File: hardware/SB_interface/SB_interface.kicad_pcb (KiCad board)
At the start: 2 copper layers, 235 parts, among them J1 8P8C_TelPairs, J2 8P8C_TelPairs, J3 8P8C_TelPairs, J4 Conn_01x10_Pin, J5 Screw_Terminal_01x02, J6 Screw_Terminal_01x02, J7 Jack-DC, K1 J104D2C12VDC.36S, K10 J104D2C12VDC.36S, K11 J104D2C12VDC.36S, K12 J104D2C12VDC.36S, K13 J104D2C12VDC.36S, K2 J104D2C12VDC.36S, K3 J104D2C12VDC.36S, K4 J104D2C12VDC.36S, K5 J104D2C12VDC.36S, K6 J104D2C12VDC.36S, K7 J104D2C12VDC.36S, K8 J104D2C12VDC.36S, K9 J104D2C12VDC.36S, Q1 2N7002, Q10 2N7002, Q11 2N7002, Q12 2N7002, Q13 2N7002, Q14 MMBTA42, Q15 MMBTA42, Q16 MMBTA42, Q17 MMBTA42, Q18 MMBTA42, Q19 MMBTA42, Q2 2N7002, Q20 MMBTA42, Q21 MMBTA42, Q22 MMBTA42, Q23 MMBTA42, Q24 MMBTA42, Q25 MMBTA42, Q26 MMBTA42, Q27 MMBTA42, Q28 MMBTA42, Q29 MMBTA42, Q3 2N7002, Q30 MMBTA42, Q31 MMBTA42, Q32 MMBTA42, Q33 MMBTA42, Q34 MMBTA42, Q35 MMBTA42, Q36 MMBTA42, Q37 MMBTA42, Q4 2N7002, Q5 2N7002, Q6 2N7002, Q7 2N7002, Q8 2N7002, Q9 2N7002, U1 MCP23017_SP, U2 MCP23017_SP

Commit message: replicated layout + added JLCPCB Design rules file
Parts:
- removed D50, D55, D60: 1N4148WS, Diode_SMD:D_SOD-323
- removed D51, D56, D61: Yellow, PCM_JLCPCB:D_0805
- removed D54, D59: 1SMA4729A, PCM_JLCPCB:D_SMA
- removed JP16, JP18: SolderJumper_2_Bridged, Jumper:SolderJumper-2_P1.3mm_Bridged_Pad1.0x1.5mm
- removed JP17, JP19, JP20: SolderJumper_2_Open, Jumper:SolderJumper-2_P1.3mm_Open_Pad1.0x1.5mm
- removed R77, R78, R79, R80, R81, R82, R83, R84, R85, R86, R87, R88: 2.2kΩ, PCM_JLCPCB:R_0805
- added C13: C, Capacitor_SMD:C_0805_2012Metric_Pad1.18x1.45mm_HandSolder, F.Cu at (185.8, 127.2)
- added C14: C, Capacitor_SMD:C_0805_2012Metric_Pad1.18x1.45mm_HandSolder, F.Cu at (165.7, 57.4)
- added D32: 1N4148WS, Diode_SMD:D_SOD-323, F.Cu at (133.4, 196.2)
- added D33: Yellow, PCM_JLCPCB:D_0805, F.Cu at (130.5, 194.1)
- added D37: Yellow, PCM_JLCPCB:D_0805, F.Cu at (15.5, 133.6)
- added D38: 1SMA4729A, PCM_JLCPCB:D_SMA, F.Cu at (87.2, 151.0)
- added D42: 1SMA4729A, PCM_JLCPCB:D_SMA, F.Cu at (155.0, 125.8)
- added D43: 1SMA4729A, PCM_JLCPCB:D_SMA, F.Cu at (155.0, 132.4)
- added D47: 1SMA4729A, PCM_JLCPCB:D_SMA, F.Cu at (135.0, 62.6)
- added D48: 1N4148WS, Diode_SMD:D_SOD-323, F.Cu at (128.9, 59.1)
- added JP10: Jumper_2_Small_Open, Connector_PinHeader_2.54mm:PinHeader_1x02_P2.54mm_Vertical, F.Cu at (9.97, -88.8)
- added JP11: Jumper_2_Small_Open, Connector_PinHeader_2.54mm:PinHeader_1x02_P2.54mm_Vertical, F.Cu at (14.6, -88.8)
- added JP12: Jumper_2_Small_Open, Connector_PinHeader_2.54mm:PinHeader_1x02_P2.54mm_Vertical, F.Cu at (0.67, -81.6)
- added JP13: Jumper_2_Small_Open, Connector_PinHeader_2.54mm:PinHeader_1x02_P2.54mm_Vertical, F.Cu at (5.32, -81.6)
- added JP14: Jumper_2_Small_Open, Connector_PinHeader_2.54mm:PinHeader_1x02_P2.54mm_Vertical, F.Cu at (9.97, -81.6)
- added R42: 180Ω, PCM_JLCPCB:R_2010, F.Cu at (119.6, 252.2)
- added R43: 180Ω, PCM_JLCPCB:R_2010, F.Cu at (113.1, 252.2)
- added R46: 2.2kΩ, PCM_JLCPCB:R_0805, F.Cu at (87.3, 261.4)
- added R47: 470kΩ, PCM_JLCPCB:R_0805, F.Cu at (158.0, 197.9)
- added R48: 180Ω, PCM_JLCPCB:R_2010, F.Cu at (162.8, 190.2)
- added R51: 4.7kΩ, PCM_JLCPCB:R_0805, F.Cu at (122.1, 196.2)
- added R52: 2.2kΩ, PCM_JLCPCB:R_0805, F.Cu at (130.5, 199.4)
- added R53: 470kΩ, PCM_JLCPCB:R_0805, F.Cu at (43.0, 137.4)
- added R56: R, Resistor_SMD:R_0805_2012Metric_Pad1.20x1.40mm_HandSolder, F.Cu at (52.3, 134.1)
- added R57: 4.7kΩ, PCM_JLCPCB:R_0805, F.Cu at (7.11, 135.7)
- added R58: 2.2kΩ, PCM_JLCPCB:R_0805, F.Cu at (15.5, 138.9)
- added R64: 2.2kΩ, PCM_JLCPCB:R_0805, F.Cu at (78.2, 157.2)
- C1, C2: value C -> 100nF; footprint Capacitor_SMD:C_0805_2012Metric_Pad1.18x1.45mm_HandSolder -> PCM_JLCPCB:C_0805
- D10, D15, D30, D35: value 1N4148WS -> 1SMA4729A; footprint Diode_SMD:D_SOD-323 -> PCM_JLCPCB:D_SMA
- D11, D26, D31, D46: value Yellow -> 1SMA4729A; footprint PCM_JLCPCB:D_0805 -> PCM_JLCPCB:D_SMA
- D12, D24, D28, D4, D44: value 1SMA4729A -> 1N4148WS; footprint PCM_JLCPCB:D_SMA -> Diode_SMD:D_SOD-323
- D13, D17, D29, D49, D5: value 1SMA4729A -> Yellow; footprint PCM_JLCPCB:D_SMA -> PCM_JLCPCB:D_0805
- D16, D36: value Yellow -> 1N4148WS; footprint PCM_JLCPCB:D_0805 -> Diode_SMD:D_SOD-323
- D25, D45: value 1N4148WS -> Yellow; footprint Diode_SMD:D_SOD-323 -> PCM_JLCPCB:D_0805
- J4: value Conn_01x10_Pin -> Screw_Terminal_01x02; footprint Connector_PinHeader_2.54mm:PinHeader_1x10_P2.54mm_Vertical -> TerminalBlock_Phoenix:TerminalBlock_Phoenix_PT-1,5-2-3.5-H_1x02_P3.50mm_Horizontal
- J6: value Screw_Terminal_01x02 -> Conn_01x10_Pin; footprint TerminalBlock_Phoenix:TerminalBlock_Phoenix_PT-1,5-2-3.5-H_1x02_P3.50mm_Horizontal -> Connector_PinHeader_2.54mm:PinHeader_1x10_P2.54mm_Vertical
- JP1: value SolderJumper_2_Bridged -> SolderJumper_2_Open; footprint Jumper:SolderJumper-2_P1.3mm_Bridged_Pad1.0x1.5mm -> Jumper:SolderJumper-2_P1.3mm_Open_Pad1.0x1.5mm
- JP15, JP5, JP8: value SolderJumper_2_Bridged -> Jumper_2_Small_Open; footprint Jumper:SolderJumper-2_P1.3mm_Bridged_Pad1.0x1.5mm -> Connector_PinHeader_2.54mm:PinHeader_1x02_P2.54mm_Vertical
- JP4, JP6, JP7, JP9: value SolderJumper_2_Open -> Jumper_2_Small_Open; footprint Jumper:SolderJumper-2_P1.3mm_Open_Pad1.0x1.5mm -> Connector_PinHeader_2.54mm:PinHeader_1x02_P2.54mm_Vertical
- K10, K11, K12, K13, K2, K4, K5, K6, K7, K8, K9: moved to B.Cu
- Q11, Q12, Q2, Q3, Q5, Q6, Q8, Q9: value 2N7002 -> MMBTA42
- Q16, Q19, Q22, Q25, Q28, Q31, Q34, Q37: value MMBTA42 -> 2N7002
- R10, R40: value 4.7kΩ -> 2.2kΩ
- R11, R17, R23, R41, R5: value 180Ω -> 470kΩ; footprint PCM_JLCPCB:R_2010 -> PCM_JLCPCB:R_0805
- R16, R22, R28: value 180Ω -> 2.2kΩ; footprint PCM_JLCPCB:R_2010 -> PCM_JLCPCB:R_0805
- R19, R24, R49, R54, R7: value R -> 180Ω; footprint Resistor_SMD:R_0805_2012Metric_Pad1.20x1.40mm_HandSolder -> PCM_JLCPCB:R_2010
- R2, R3: value 180Ω -> 1kΩ; footprint PCM_JLCPCB:R_2010 -> PCM_JLCPCB:R_0805
- R20, R50, R8: value 4.7kΩ -> R; footprint PCM_JLCPCB:R_0805 -> Resistor_SMD:R_0805_2012Metric_Pad1.20x1.40mm_HandSolder
- R21, R27, R33, R9: value 180Ω -> 4.7kΩ; footprint PCM_JLCPCB:R_2010 -> PCM_JLCPCB:R_0805
- R25, R30, R55: value 4.7kΩ -> 180Ω; footprint PCM_JLCPCB:R_0805 -> PCM_JLCPCB:R_2010
- R26, R32, R38: value 180Ω -> R; footprint PCM_JLCPCB:R_2010 -> Resistor_SMD:R_0805_2012Metric_Pad1.20x1.40mm_HandSolder
- R29, R59: value R -> 470kΩ; footprint Resistor_SMD:R_0805_2012Metric_Pad1.20x1.40mm_HandSolder -> PCM_JLCPCB:R_0805
- R34: value R -> 2.2kΩ; footprint Resistor_SMD:R_0805_2012Metric_Pad1.20x1.40mm_HandSolder -> PCM_JLCPCB:R_0805
- R35: value 4.7kΩ -> 470kΩ
- R39: value R -> 4.7kΩ; footprint Resistor_SMD:R_0805_2012Metric_Pad1.20x1.40mm_HandSolder -> PCM_JLCPCB:R_0805
- R4: value R -> 1kΩ; footprint Resistor_SMD:R_0805_2012Metric_Pad1.20x1.40mm_HandSolder -> PCM_JLCPCB:R_0805
- R60, R61: value 1kΩ -> 180Ω; footprint PCM_JLCPCB:R_0805 -> PCM_JLCPCB:R_2010
- R62: value 1kΩ -> R; footprint PCM_JLCPCB:R_0805 -> Resistor_SMD:R_0805_2012Metric_Pad1.20x1.40mm_HandSolder
- R66, R67, R72, R73: value 470kΩ -> 180Ω; footprint PCM_JLCPCB:R_0805 -> PCM_JLCPCB:R_2010
- R68, R74: value 470kΩ -> R; footprint PCM_JLCPCB:R_0805 -> Resistor_SMD:R_0805_2012Metric_Pad1.20x1.40mm_HandSolder
- R69, R75: value 470kΩ -> 4.7kΩ
- R70, R76: value 470kΩ -> 2.2kΩ
- moved C3 341.4 mm to (261.4, 26.1), turned to 90 degrees
- moved R5 334.8 mm to (249.2, 29.3)
- moved Q5 332.3 mm to (273.0, 142.9), turned to -90 degrees
- moved R14 321.9 mm to (282.2, 142.8), turned to -90 degrees
- moved C4 321.4 mm to (285.1, 142.8), turned to 90 degrees
- moved K7 317.5 mm to (-46.4, 259.2), turned to 180 degrees
- moved Q4 317.2 mm to (217.4, 27.7)
- moved Q19 316.6 mm to (-51.0, 255.1)
- moved D13 315.0 mm to (-45.1, 165.0), turned to -90 degrees
- moved D23 310.7 mm to (-37.8, 258.7)
- moved D4 309.5 mm to (224.5, 27.7), turned to 90 degrees
- moved R6 303.9 mm to (254.0, 21.7), turned to 180 degrees
- moved C6 302.0 mm to (-13.8, 86.9), turned to 90 degrees
- moved DB6 301.5 mm to (-27.7, 255.4), turned to 90 degrees
- moved D6 297.8 mm to (254.3, 141.4)
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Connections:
- C1 pad 1: /RING_1 -> +3.3V
- C10 pad 1: /RING_9 -> /RING_7
- C11 pad 1: /RING_10 -> /RING_8
- C12 pad 1: /RING_11 -> /RING_9
- C2 pad 1: /RING_0 -> +3.3V
- C3 pad 1: /RING_2 -> /RING_1
- C4 pad 1: /RING_3 -> /RING_0
- C5 pad 1: /RING_4 -> /RING_2
- C6 pad 1: /RING_5 -> /RING_3
- C7 pad 1: /RING_6 -> /RING_4
- C8 pad 1: /RING_7 -> /RING_5
- C9 pad 1: /RING_8 -> /RING_6
- D10 pad 1: +12V -> /RelayAndRingDetect2/Tel_B
- D10 pad 2: Net-(D10-A) -> Net-(D10-Pad2)
- D11 pad 1: Net-(D10-A) -> /RelayAndRingDetect2/Tel_A
- D12 pad 1: /RelayAndRingDetect4/Tel_B -> +12V
- D12 pad 2: Net-(D12-Pad2) -> Net-(D12-A)
- D13 pad 1: /RelayAndRingDetect5/Tel_B -> Net-(D12-A)
- D14 pad 1: /RelayAndRingDetect2/Tel_A -> /RelayAndRingDetect3/Tel_B
- D15 pad 1: +12V -> /RelayAndRingDetect3/Tel_A
- D15 pad 2: Net-(D15-A) -> Net-(D15-Pad2)
- D16 pad 1: Net-(D15-A) -> +12V
- D16 pad 2: Net-(D16-Pad2) -> Net-(D16-A)
- D17 pad 1: /RelayAndRingDetect6/Tel_B -> Net-(D16-A)
- D18 pad 1: /RelayAndRingDetect7/Tel_B -> /RelayAndRingDetect4/Tel_B
- D19 pad 1: /RelayAndRingDetect3/Tel_A -> /RelayAndRingDetect4/Tel_A
- D22 pad 1: /RelayAndRingDetect8/Tel_B -> /RelayAndRingDetect5/Tel_B
- D23 pad 1: /RelayAndRingDetect9/Tel_B -> /RelayAndRingDetect5/Tel_A
- D24 pad 1: /RelayAndRingDetect4/Tel_A -> +12V
- D24 pad 2: Net-(D24-Pad2) -> Net-(D24-A)
- D25 pad 1: +12V -> Net-(D24-A)
- D25 pad 2: Net-(D25-A) -> Net-(D25-Pad2)
- D26 pad 1: Net-(D25-A) -> /RelayAndRingDetect6/Tel_B
- D27 pad 1: /RelayAndRingDetect10/Tel_B -> /RelayAndRingDetect6/Tel_A
- D28 pad 1: /RelayAndRingDetect11/Tel_B -> +12V
- D28 pad 2: Net-(D28-Pad2) -> Net-(D28-A)
- D29 pad 1: /RelayAndRingDetect5/Tel_A -> Net-(D28-A)
- D3 pad 1: /RelayAndRingDetect0/Tel_B -> /RelayAndRingDetect1/Tel_A
- D30 pad 1: +12V -> /RelayAndRingDetect7/Tel_B
- D30 pad 2: Net-(D30-A) -> Net-(D30-Pad2)
- D31 pad 1: Net-(D30-A) -> /RelayAndRingDetect7/Tel_A
- D34 pad 1: /RelayAndRingDetect6/Tel_A -> /RelayAndRingDetect8/Tel_B
- D35 pad 1: +12V -> /RelayAndRingDetect8/Tel_A
- D35 pad 2: Net-(D35-A) -> Net-(D35-Pad2)
- D36 pad 1: Net-(D35-A) -> +12V
- D36 pad 2: Net-(D36-Pad2) -> Net-(D36-A)
- D39 pad 1: /RelayAndRingDetect7/Tel_A -> /RelayAndRingDetect9/Tel_A
- D4 pad 1: /RelayAndRingDetect2/Tel_B -> +12V
- D4 pad 2: Net-(D4-Pad2) -> Net-(D4-A)
- D44 pad 1: /RelayAndRingDetect8/Tel_A -> +12V
- D44 pad 2: Net-(D44-Pad2) -> Net-(D44-A)
- D45 pad 1: +12V -> Net-(D44-A)
- D45 pad 2: Net-(D45-A) -> Net-(D45-Pad2)
- D46 pad 1: Net-(D45-A) -> /RelayAndRingDetect11/Tel_B
- D49 pad 1: /RelayAndRingDetect9/Tel_A -> Net-(D48-A)
- D5 pad 1: /RelayAndRingDetect1/Tel_A -> Net-(D4-A)
- D6 pad 1: /RelayAndRingDetect3/Tel_B -> /RelayAndRingDetect0/Tel_B
- DB1 pad 4: Net-(D5-Pad2) -> Net-(D3-Pad2)
- DB10 pad 3: Net-(D23-Pad2) -> Net-(D38-Pad2)
- DB10 pad 4: Net-(D49-Pad2) -> Net-(D39-Pad2)
- DB11 pad 3: Net-(D27-Pad2) -> Net-(D42-Pad2)
- DB12 pad 3: Net-(D28-Pad2) -> Net-(D46-Pad2)
- DB2 pad 3: Net-(D3-Pad2) -> Net-(D6-Pad2)
- DB3 pad 3: Net-(D4-Pad2) -> Net-(D10-Pad2)
- DB3 pad 4: Net-(D14-Pad2) -> Net-(D11-Pad2)
- DB4 pad 3: Net-(D6-Pad2) -> Net-(D14-Pad2)
- DB4 pad 4: Net-(D19-Pad2) -> Net-(D15-Pad2)
- DB5 pad 3: Net-(D12-Pad2) -> Net-(D18-Pad2)
- DB5 pad 4: Net-(D24-Pad2) -> Net-(D19-Pad2)
- DB6 pad 3: Net-(D13-Pad2) -> Net-(D22-Pad2)
- DB6 pad 4: Net-(D29-Pad2) -> Net-(D23-Pad2)
- DB7 pad 3: Net-(D17-Pad2) -> Net-(D26-Pad2)
- DB7 pad 4: Net-(D34-Pad2) -> Net-(D27-Pad2)
- DB8 pad 3: Net-(D18-Pad2) -> Net-(D30-Pad2)
- DB8 pad 4: Net-(D39-Pad2) -> Net-(D31-Pad2)
- DB9 pad 3: Net-(D22-Pad2) -> Net-(D34-Pad2)
- DB9 pad 4: Net-(D44-Pad2) -> Net-(D35-Pad2)
- J4 pad 1: /SDA -> /AUX_A
- J4 pad 2: /SCL -> /AUX_B
- J6 pad 1: /AUX_A -> /SDA
- J6 pad 2: /AUX_B -> /SCL
- JP1 pad 1: +3.3V -> /INTB_1
- JP1 pad 2: Net-(JP1-B) -> /INTA_1
- JP15 pad 1: Net-(JP15-A) -> GND
- JP15 pad 2: GND -> Net-(JP14-A)
- JP2 pad 1: /INTB_1 -> /INTA_2
- JP2 pad 2: /INTA_1 -> /INTB_1
- JP3 pad 1: GND -> /INTB_2
- JP3 pad 2: Net-(JP1-B) -> /INTA_2
- JP4 pad 1: /INTA_2 -> Net-(JP4-A)
- JP4 pad 2: /INTB_1 -> +3.3V
- JP5 pad 1: +3.3V -> GND
- JP5 pad 2: Net-(JP5-B) -> Net-(JP4-A)
- JP6 pad 1: /INTB_2 -> Net-(JP6-A)
- JP6 pad 2: /INTA_2 -> +3.3V
- JP7 pad 2: Net-(JP5-B) -> Net-(JP6-A)
- JP8 pad 1: +3.3V -> Net-(JP8-A)
- JP8 pad 2: Net-(JP8-B) -> +3.3V
- JP9 pad 2: Net-(JP8-B) -> Net-(JP8-A)
- K10 pad A2: Net-(D45-A) -> Net-(D36-A)
- K11 pad A2: Net-(D50-A) -> Net-(D40-A)
- K12 pad A2: Net-(D55-A) -> Net-(D44-A)
- K13 pad A2: Net-(D60-A) -> Net-(D48-A)
- K2 pad A2: Net-(D10-A) -> Net-(D4-A)
- K4 pad A2: Net-(D15-A) -> Net-(D12-A)
- K5 pad A2: Net-(D20-A) -> Net-(D16-A)
- K6 pad A2: Net-(D25-A) -> Net-(D20-A)
- K7 pad A2: Net-(D30-A) -> Net-(D24-A)
- K8 pad A2: Net-(D35-A) -> Net-(D28-A)
- K9 pad A2: Net-(D40-A) -> Net-(D32-A)
- Q10 pad 1: /SEL_PORT_8 -> /SEL_PORT_2
- Q10 pad 3: Net-(D45-A) -> Net-(D12-A)
- Q11 pad 1: /SEL_PORT_9 -> Net-(Q11-B)
- Q11 pad 2: GND -> Net-(DB4--)
- Q11 pad 3: Net-(D50-A) -> Net-(Q11-C)
- Q12 pad 1: /SEL_PORT_10 -> Net-(Q11-C)
- Q12 pad 2: GND -> Net-(Q11-B)
- Q12 pad 3: Net-(D55-A) -> Net-(OP4-CAT)
- Q13 pad 1: /SEL_PORT_11 -> /SEL_PORT_3
- Q13 pad 3: Net-(D60-A) -> Net-(D16-A)
- Q14 pad 2: Net-(Q14-E) -> Net-(DB5--)
- Q14 pad 3: Net-(OP1-CAT) -> Net-(Q14-C)
- Q15 pad 1: Net-(Q15-B) -> Net-(Q14-C)
- Q15 pad 2: Net-(Q15-E) -> Net-(Q14-B)
- Q15 pad 3: Net-(OP2-CAT) -> Net-(OP5-CAT)
- Q16 pad 1: Net-(Q16-B) -> /SEL_PORT_4
- Q16 pad 2: Net-(Q16-E) -> GND
- Q16 pad 3: Net-(OP3-CAT) -> Net-(D20-A)
- Q17 pad 2: Net-(Q17-E) -> Net-(DB6--)
- Q17 pad 3: Net-(OP4-CAT) -> Net-(Q17-C)
- Q18 pad 1: Net-(Q18-B) -> Net-(Q17-C)
- Q18 pad 2: Net-(Q18-E) -> Net-(Q17-B)
- Q18 pad 3: Net-(OP5-CAT) -> Net-(OP6-CAT)
- Q19 pad 1: Net-(Q19-B) -> /SEL_PORT_5
- Q19 pad 2: Net-(Q19-E) -> GND
- Q19 pad 3: Net-(OP6-CAT) -> Net-(D24-A)
- Q2 pad 1: /SEL_PORT_1 -> Net-(Q2-B)
- Q2 pad 2: GND -> Net-(DB1--)
- Q2 pad 3: Net-(D10-A) -> Net-(Q2-C)
- Q20 pad 2: Net-(Q20-E) -> Net-(DB7--)
- Q20 pad 3: Net-(OP7-CAT) -> Net-(Q20-C)
- Q21 pad 1: Net-(Q21-B) -> Net-(Q20-C)
- Q21 pad 2: Net-(Q21-E) -> Net-(Q20-B)
- Q21 pad 3: Net-(OP8-CAT) -> Net-(OP7-CAT)
- Q22 pad 1: Net-(Q22-B) -> /SEL_PORT_6
- Q22 pad 2: Net-(Q22-E) -> GND
- Q22 pad 3: Net-(OP9-CAT) -> Net-(D28-A)
- Q23 pad 2: Net-(Q23-E) -> Net-(DB8--)
- Q23 pad 3: Net-(OP10-CAT) -> Net-(Q23-C)
- Q24 pad 1: Net-(Q24-B) -> Net-(Q23-C)
- Q24 pad 2: Net-(Q24-E) -> Net-(Q23-B)
- Q24 pad 3: Net-(OP11-CAT) -> Net-(OP8-CAT)
- Q25 pad 1: Net-(Q25-B) -> /SEL_PORT_7
- Q25 pad 2: Net-(Q25-E) -> GND
- Q25 pad 3: Net-(OP12-CAT) -> Net-(D32-A)
- Q26 pad 1: Net-(Q14-E) -> Net-(Q26-B)
- Q26 pad 2: Net-(DB1--) -> Net-(DB9--)
- Q26 pad 3: Net-(Q14-B) -> Net-(Q26-C)
- Q27 pad 1: Net-(Q15-E) -> Net-(Q26-C)
- Q27 pad 2: Net-(DB2--) -> Net-(Q26-B)
- Q27 pad 3: Net-(Q15-B) -> Net-(OP9-CAT)
- Q28 pad 1: Net-(Q16-E) -> /SEL_PORT_8
- Q28 pad 2: Net-(DB3--) -> GND
- Q28 pad 3: Net-(Q16-B) -> Net-(D36-A)
- Q29 pad 1: Net-(Q17-E) -> Net-(Q29-B)
- Q29 pad 2: Net-(DB4--) -> Net-(DB10--)
- Q29 pad 3: Net-(Q17-B) -> Net-(Q29-C)
- Q3 pad 1: /SEL_PORT_0 -> Net-(Q2-C)
- Q3 pad 2: GND -> Net-(Q2-B)
- Q3 pad 3: Net-(D8-A) -> Net-(OP1-CAT)
- Q30 pad 1: Net-(Q18-E) -> Net-(Q29-C)
- Q30 pad 2: Net-(DB5--) -> Net-(Q29-B)
- Q30 pad 3: Net-(Q18-B) -> Net-(OP10-CAT)
- Q31 pad 1: Net-(Q19-E) -> /SEL_PORT_9
- Q31 pad 2: Net-(DB6--) -> GND
- Q31 pad 3: Net-(Q19-B) -> Net-(D40-A)
- Q32 pad 1: Net-(Q20-E) -> Net-(Q32-B)
- Q32 pad 2: Net-(DB7--) -> Net-(DB11--)
- Q32 pad 3: Net-(Q20-B) -> Net-(Q32-C)
- Q33 pad 1: Net-(Q21-E) -> Net-(Q32-C)
- Q33 pad 2: Net-(DB8--) -> Net-(Q32-B)
- Q33 pad 3: Net-(Q21-B) -> Net-(OP11-CAT)
- Q34 pad 1: Net-(Q22-E) -> /SEL_PORT_10
- Q34 pad 2: Net-(DB9--) -> GND
- Q34 pad 3: Net-(Q22-B) -> Net-(D44-A)
- Q35 pad 1: Net-(Q23-E) -> Net-(Q35-B)
- Q35 pad 2: Net-(DB10--) -> Net-(DB12--)
- Q35 pad 3: Net-(Q23-B) -> Net-(Q35-C)
- Q36 pad 1: Net-(Q24-E) -> Net-(Q35-C)
- Q36 pad 2: Net-(DB11--) -> Net-(Q35-B)
- Q36 pad 3: Net-(Q24-B) -> Net-(OP12-CAT)
- Q37 pad 1: Net-(Q25-E) -> /SEL_PORT_11
- Q37 pad 2: Net-(DB12--) -> GND
- Q37 pad 3: Net-(Q25-B) -> Net-(D48-A)
- Q4 pad 1: /SEL_PORT_2 -> /SEL_PORT_1
- Q4 pad 3: Net-(D15-A) -> Net-(D4-A)
- Q5 pad 1: /SEL_PORT_3 -> Net-(Q5-B)
- Q5 pad 2: GND -> Net-(DB2--)
- Q5 pad 3: Net-(D20-A) -> Net-(Q5-C)
- Q6 pad 1: /SEL_PORT_4 -> Net-(Q5-C)
- Q6 pad 2: GND -> Net-(Q5-B)
- Q6 pad 3: Net-(D25-A) -> Net-(OP2-CAT)
- Q7 pad 1: /SEL_PORT_5 -> /SEL_PORT_0
- Q7 pad 3: Net-(D30-A) -> Net-(D8-A)
- Q8 pad 1: /SEL_PORT_6 -> Net-(Q8-B)
- Q8 pad 2: GND -> Net-(DB3--)
- Q8 pad 3: Net-(D35-A) -> Net-(Q8-C)
- Q9 pad 1: /SEL_PORT_7 -> Net-(Q8-C)
- Q9 pad 2: GND -> Net-(Q8-B)
- Q9 pad 3: Net-(D40-A) -> Net-(OP3-CAT)
- R10 pad 1: /SEL_PORT_1 -> +12V
- R10 pad 2: GND -> Net-(D5-Pad2)
- R11 pad 1: Net-(R11-Pad1) -> Net-(DB2-+)
- R11 pad 2: Net-(DB2--) -> Net-(Q5-C)
- R12 pad 1: Net-(Q18-E) -> Net-(Q5-B)
- R13 pad 1: Net-(Q19-E) -> Net-(R12-Pad2)
- R13 pad 2: Net-(R13-Pad2) -> Net-(DB2--)
- R14 pad 2: /RING_2 -> /RING_0
- R15 pad 1: /SEL_PORT_2 -> /SEL_PORT_0
- R16 pad 1: Net-(R16-Pad1) -> +12V
- R16 pad 2: Net-(DB3--) -> Net-(D9-Pad2)
- R17 pad 1: Net-(Q20-E) -> Net-(DB3-+)
- R17 pad 2: Net-(R17-Pad2) -> Net-(Q8-C)
- R18 pad 1: Net-(Q21-E) -> Net-(Q8-B)
- R19 pad 1: +3.3V -> Net-(R18-Pad2)
- R19 pad 2: /RING_3 -> Net-(DB3--)
- R2 pad 1: Net-(Q14-E) -> +3.3V
- R2 pad 2: Net-(R2-Pad2) -> /SCL
- R20 pad 1: /SEL_PORT_3 -> +3.3V
- R20 pad 2: GND -> /RING_2
- R21 pad 1: Net-(R21-Pad1) -> /SEL_PORT_2
- R21 pad 2: Net-(DB4--) -> GND
- R22 pad 1: Net-(Q22-E) -> +12V
- R22 pad 2: Net-(R22-Pad2) -> Net-(D13-Pad2)
- R23 pad 1: Net-(Q23-E) -> Net-(DB4-+)
- R23 pad 2: Net-(R23-Pad2) -> Net-(Q11-C)
- R24 pad 1: +3.3V -> Net-(Q11-B)
- R24 pad 2: /RING_4 -> Net-(R24-Pad2)
- R25 pad 1: /SEL_PORT_4 -> Net-(R24-Pad2)
- R25 pad 2: GND -> Net-(DB4--)
- R26 pad 1: Net-(R12-Pad2) -> +3.3V
- R26 pad 2: Net-(DB5--) -> /RING_3
- R27 pad 1: Net-(Q24-E) -> /SEL_PORT_3
- R27 pad 2: Net-(R27-Pad2) -> GND
- R28 pad 1: Net-(Q25-E) -> +12V
- R28 pad 2: Net-(R28-Pad2) -> Net-(D17-Pad2)
- R29 pad 1: +3.3V -> Net-(DB5-+)
- R29 pad 2: /RING_5 -> Net-(Q14-C)
- R3 pad 1: Net-(Q15-E) -> +3.3V
- R3 pad 2: Net-(R11-Pad1) -> /SDA
- R30 pad 1: /SEL_PORT_5 -> Net-(Q14-B)
- R30 pad 2: GND -> Net-(R30-Pad2)
- R31 pad 1: Net-(R13-Pad2) -> Net-(R30-Pad2)
- R31 pad 2: Net-(DB6--) -> Net-(DB5--)
- R32 pad 1: Net-(R17-Pad2) -> +3.3V
- R32 pad 2: Net-(DB7--) -> /RING_4
- R33 pad 1: Net-(R18-Pad2) -> /SEL_PORT_4
- R33 pad 2: Net-(DB8--) -> GND
- R34 pad 1: +3.3V -> +12V
- R34 pad 2: /RING_6 -> Net-(D21-Pad2)
- R35 pad 1: /SEL_PORT_6 -> Net-(DB6-+)
- R35 pad 2: GND -> Net-(Q17-C)
- R36 pad 1: Net-(R22-Pad2) -> Net-(Q17-B)
- R36 pad 2: Net-(DB9--) -> Net-(R36-Pad2)
- R37 pad 1: Net-(R23-Pad2) -> Net-(R36-Pad2)
- R37 pad 2: Net-(DB10--) -> Net-(DB6--)
- R38 pad 1: Net-(R27-Pad2) -> +3.3V
- R38 pad 2: Net-(DB11--) -> /RING_5
- R39 pad 1: +3.3V -> /SEL_PORT_5
- R39 pad 2: /RING_7 -> GND
- R4 pad 2: /RING_1 -> /RESET
- R40 pad 1: /SEL_PORT_7 -> +12V
- R40 pad 2: GND -> Net-(D25-Pad2)
- R41 pad 1: Net-(R28-Pad2) -> Net-(DB7-+)
- R41 pad 2: Net-(DB12--) -> Net-(Q20-C)
- R44 pad 2: /RING_8 -> /RING_6
- R45 pad 1: /SEL_PORT_8 -> /SEL_PORT_6
- R49 pad 1: +3.3V -> Net-(R48-Pad2)
- R49 pad 2: /RING_9 -> Net-(DB8--)
- R5 pad 1: Net-(Q16-E) -> Net-(DB1-+)
- R5 pad 2: Net-(R16-Pad1) -> Net-(Q2-C)
- R50 pad 1: /SEL_PORT_9 -> +3.3V
- R50 pad 2: GND -> /RING_7
- R54 pad 1: +3.3V -> Net-(Q26-B)
- R54 pad 2: /RING_10 -> Net-(R54-Pad2)
- R55 pad 1: /SEL_PORT_10 -> Net-(R54-Pad2)
- R55 pad 2: GND -> Net-(DB9--)
- R59 pad 1: +3.3V -> Net-(DB10-+)
- R59 pad 2: /RING_11 -> Net-(Q29-C)
- R6 pad 1: Net-(Q17-E) -> Net-(Q2-B)
- R6 pad 2: Net-(R21-Pad1) -> Net-(R6-Pad2)
- R60 pad 1: +3.3V -> Net-(Q29-B)
- R60 pad 2: /SCL -> Net-(R60-Pad2)
- R61 pad 1: +3.3V -> Net-(R60-Pad2)
- R61 pad 2: /SDA -> Net-(DB10--)
- R62 pad 2: /RESET -> /RING_9
- R63 pad 1: /SEL_PORT_11 -> /SEL_PORT_9
- R65 pad 1: Net-(DB1-+) -> Net-(DB11-+)
- R65 pad 2: Net-(Q14-B) -> Net-(Q32-C)
- R66 pad 1: Net-(DB2-+) -> Net-(Q32-B)
- R66 pad 2: Net-(Q15-B) -> Net-(R66-Pad2)
- R67 pad 1: Net-(DB3-+) -> Net-(R66-Pad2)
- R67 pad 2: Net-(Q16-B) -> Net-(DB11--)
- R68 pad 1: Net-(DB4-+) -> +3.3V
- R68 pad 2: Net-(Q17-B) -> /RING_10
- R69 pad 1: Net-(DB5-+) -> /SEL_PORT_10
- R69 pad 2: Net-(Q18-B) -> GND
- R7 pad 1: +3.3V -> Net-(R6-Pad2)
- R7 pad 2: /RING_0 -> Net-(DB1--)
- R70 pad 1: Net-(DB6-+) -> +12V
- R70 pad 2: Net-(Q19-B) -> Net-(D45-Pad2)
- R71 pad 1: Net-(DB7-+) -> Net-(DB12-+)
- R71 pad 2: Net-(Q20-B) -> Net-(Q35-C)
- R72 pad 1: Net-(DB8-+) -> Net-(Q35-B)
- R72 pad 2: Net-(Q21-B) -> Net-(R72-Pad2)
- R73 pad 1: Net-(DB9-+) -> Net-(R72-Pad2)
- R73 pad 2: Net-(Q22-B) -> Net-(DB12--)
- R74 pad 1: Net-(DB10-+) -> +3.3V
- R74 pad 2: Net-(Q23-B) -> /RING_11
- R75 pad 1: Net-(DB11-+) -> /SEL_PORT_11
- R75 pad 2: Net-(Q24-B) -> GND
- R76 pad 1: Net-(DB12-+) -> +12V
- R76 pad 2: Net-(Q25-B) -> Net-(D49-Pad2)
- R8 pad 1: /SEL_PORT_0 -> +3.3V
- R8 pad 2: GND -> /RING_1
- R9 pad 1: Net-(R2-Pad2) -> /SEL_PORT_1
- R9 pad 2: Net-(DB1--) -> GND
- U1 pad 15: Net-(JP8-B) -> Net-(JP12-A)
- U1 pad 16: Net-(JP5-B) -> Net-(JP8-A)
- U1 pad 17: Net-(JP1-B) -> Net-(JP4-A)
- U2 pad 15: Net-(JP15-A) -> Net-(JP14-A)
- U2 pad 17: Net-(JP16-B) -> Net-(JP6-A)
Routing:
- net +12V: track 10.0 -> 70.9 mm
- net Net-(Q15-E): track 27.2 -> 0.00 mm
- net /RelayAndRingDetect1/Tel_A: track 0.00 -> 14.1 mm
- net /RelayAndRingDetect5/Tel_B: track 0.00 -> 14.0 mm
- net /RelayAndRingDetect4/Tel_B: track 0.00 -> 14.0 mm
- net /RelayAndRingDetect1/Tel_B: track 0.00 -> 14.0 mm
- net /RelayAndRingDetect9/Tel_B: track 0.00 -> 14.0 mm
- net /RelayAndRingDetect7/Tel_B: track 0.00 -> 14.0 mm
- net /RelayAndRingDetect10/Tel_B: track 0.00 -> 14.0 mm
- net /RelayAndRingDetect3/Tel_B: track 0.00 -> 14.0 mm
- net /RelayAndRingDetect11/Tel_B: track 0.00 -> 14.0 mm
- net /RelayAndRingDetect8/Tel_B: track 0.00 -> 14.0 mm
- net /RelayAndRingDetect2/Tel_B: track 0.00 -> 14.0 mm
- net /RelayAndRingDetect6/Tel_B: track 0.00 -> 14.0 mm
- net /RelayAndRingDetect0/Tel_A: track 14.0 -> 1.37 mm
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
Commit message: layout of tel inputs
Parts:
- removed JP10, JP11, JP12, JP13, JP14, JP15: Jumper_2_Small_Open, Connector_PinHeader_2.54mm:PinHeader_1x02_P2.54mm_Vertical
- added J8: Jack-DC, Connector_BarrelJack:BarrelJack_Horizontal, F.Cu at (185.6, 136.0)
- J4: value Screw_Terminal_01x02 -> Expansion Hdr.; footprint TerminalBlock_Phoenix:TerminalBlock_Phoenix_PT-1,5-2-3.5-H_1x02_P3.50mm_Horizontal -> Connector_PinHeader_2.54mm:PinHeader_1x08_P2.54mm_Vertical
- J6: value Conn_01x10_Pin -> Screw_Terminal_01x02; footprint Connector_PinHeader_2.54mm:PinHeader_1x10_P2.54mm_Vertical -> TerminalBlock_Phoenix:TerminalBlock_Phoenix_PT-1,5-2-3.5-H_1x02_P3.50mm_Horizontal
- J7: value Jack-DC -> Conn_01x10_Pin; footprint Connector_BarrelJack:BarrelJack_Horizontal -> Connector_PinHeader_2.54mm:PinHeader_1x10_P2.54mm_Vertical
- JP1, JP2, JP3: value SolderJumper_2_Open -> Jumper_2_Small_Open; footprint Jumper:SolderJumper-2_P1.3mm_Open_Pad1.0x1.5mm -> Connector_PinHeader_2.54mm:PinHeader_1x02_P2.54mm_Vertical
- JP4, JP5: value Jumper_2_Small_Open -> A0; footprint Connector_PinHeader_2.54mm:PinHeader_1x02_P2.54mm_Vertical -> Connector_PinHeader_2.54mm:PinHeader_1x03_P2.54mm_Vertical
- JP6, JP7: value Jumper_2_Small_Open -> A1; footprint Connector_PinHeader_2.54mm:PinHeader_1x02_P2.54mm_Vertical -> Connector_PinHeader_2.54mm:PinHeader_1x03_P2.54mm_Vertical
- JP8, JP9: value Jumper_2_Small_Open -> A2; footprint Connector_PinHeader_2.54mm:PinHeader_1x02_P2.54mm_Vertical -> Connector_PinHeader_2.54mm:PinHeader_1x03_P2.54mm_Vertical
- moved JP3 294.6 mm to (189.0, 162.2), turned to -90 degrees
- moved JP2 293.7 mm to (189.0, 157.6), turned to -90 degrees
- moved JP1 292.9 mm to (189.0, 152.9), turned to -90 degrees
- moved JP5 291.9 mm to (160.5, 151.3)
- moved JP9 289.9 mm to (167.9, 151.3)
- moved JP7 289.0 mm to (164.2, 151.3)
- moved U2 270.8 mm to (147.2, 123.7)
- moved JP4 267.8 mm to (170.8, 110.9)
- moved JP8 267.1 mm to (178.2, 110.9)
- moved JP6 264.3 mm to (174.5, 110.9)
- moved J7 263.7 mm to (258.3, 59.7)
- moved J4 252.0 mm to (160.3, 141.5), turned to 180 degrees
- moved U1 245.4 mm to (147.2, 81.8)
- moved J3 235.3 mm to (45.3, 120.3), turned to -90 degrees
- moved C1 232.4 mm to (184.1, 78.0)
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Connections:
- net Net-(OP1-CAT) renamed /RelayAndRingDetect1/COOLING
- net Net-(OP10-CAT) renamed /RelayAndRingDetect9/COOLING
- net Net-(OP11-CAT) renamed /RelayAndRingDetect10/COOLING
- net Net-(OP12-CAT) renamed /RelayAndRingDetect11/COOLING
- net Net-(OP2-CAT) renamed /RelayAndRingDetect0/COOLING
- net Net-(OP3-CAT) renamed /RelayAndRingDetect2/COOLING
- net Net-(OP4-CAT) renamed /RelayAndRingDetect3/COOLING
- net Net-(OP5-CAT) renamed /RelayAndRingDetect4/COOLING
- net Net-(OP6-CAT) renamed /RelayAndRingDetect5/COOLING
- net Net-(OP7-CAT) renamed /RelayAndRingDetect6/COOLING
- net Net-(OP8-CAT) renamed /RelayAndRingDetect7/COOLING
- net Net-(OP9-CAT) renamed /RelayAndRingDetect8/COOLING
- J4 pad 1: /AUX_A -> Net-(J4-Pin_1)
- J4 pad 2: /AUX_B -> Net-(J4-Pin_2)
- J5 pad 1: /AUDIO_A -> /AUX_A
- J5 pad 2: /AUDIO_B -> /AUX_B
- J6 pad 1: /SDA -> /AUDIO_A
- J6 pad 2: /SCL -> /AUDIO_B
- J7 pad 1: +12V -> /SDA
- J7 pad 2: GND -> /SCL
- J7 pad 3: (no net) -> /RESET
- JP4 pad 1: Net-(JP4-A) -> +3.3V
- JP4 pad 2: +3.3V -> Net-(JP4-C)
- JP5 pad 1: GND -> +3.3V
- JP5 pad 2: Net-(JP4-A) -> Net-(JP5-C)
- JP6 pad 1: Net-(JP6-A) -> +3.3V
- JP6 pad 2: +3.3V -> Net-(JP6-C)
- JP7 pad 1: GND -> +3.3V
- JP7 pad 2: Net-(JP6-A) -> Net-(JP7-C)
- JP8 pad 1: Net-(JP8-A) -> +3.3V
- JP8 pad 2: +3.3V -> Net-(JP8-C)
- JP9 pad 1: GND -> +3.3V
- JP9 pad 2: Net-(JP8-A) -> Net-(JP9-C)
- U1 pad 15: Net-(JP12-A) -> Net-(JP8-C)
- U1 pad 16: Net-(JP8-A) -> Net-(JP6-C)
- U1 pad 17: Net-(JP4-A) -> Net-(JP4-C)
- U2 pad 15: Net-(JP14-A) -> Net-(JP9-C)
- U2 pad 16: Net-(JP10-A) -> Net-(JP7-C)
- U2 pad 17: Net-(JP6-A) -> Net-(JP5-C)
- U2 pad 21: unconnected-(U2-GPA0-Pad21) -> Net-(J4-Pin_1)
- U2 pad 22: unconnected-(U2-GPA1-Pad22) -> Net-(J4-Pin_2)
- U2 pad 23: unconnected-(U2-GPA2-Pad23) -> Net-(J4-Pin_3)
- U2 pad 24: unconnected-(U2-GPA3-Pad24) -> Net-(J4-Pin_4)
- U2 pad 25: unconnected-(U2-GPA4-Pad25) -> Net-(J4-Pin_5)
- U2 pad 26: unconnected-(U2-GPA5-Pad26) -> Net-(J4-Pin_6)
- U2 pad 27: unconnected-(U2-GPA6-Pad27) -> Net-(J4-Pin_7)
- U2 pad 28: unconnected-(U2-GPA7-Pad28) -> Net-(J4-Pin_8)
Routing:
- net /RelayAndRingDetect0/AUDIO_B: track 0.00 -> 212.4 mm
- net /RelayAndRingDetect0/AUDIO_A: track 0.00 -> 212.4 mm
- net /RelayAndRingDetect11/Tel_A: track 1.37 -> 124.1 mm
- net /RelayAndRingDetect0/Tel_A: track 1.37 -> 114.1 mm
- net /RelayAndRingDetect0/Tel_B: track 14.0 -> 125.7 mm
- net /RelayAndRingDetect10/Tel_A: track 1.37 -> 109.0 mm, vias 0 -> 1
- net /RelayAndRingDetect1/Tel_B: track 14.0 -> 116.1 mm, vias 0 -> 1
- net /RelayAndRingDetect11/Tel_B: track 14.0 -> 110.5 mm
- net /RelayAndRingDetect9/Tel_A: track 1.36 -> 96.6 mm, vias 0 -> 1
- net /RelayAndRingDetect1/Tel_A: track 14.1 -> 101.5 mm
- net /RelayAndRingDetect2/Tel_B: track 14.0 -> 100.9 mm, vias 0 -> 2
- net /RelayAndRingDetect10/Tel_B: track 14.0 -> 98.4 mm, vias 0 -> 1
- net /RelayAndRingDetect2/Tel_A: track 1.37 -> 83.4 mm
- net /RelayAndRingDetect8/Tel_A: track 1.37 -> 81.6 mm, vias 0 -> 1
- net /RelayAndRingDetect3/Tel_A: track 1.37 -> 76.9 mm
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- added copper zone on B.Cu, net /RelayAndRingDetect0/COOLING
- added copper zone on F.Cu, net /RelayAndRingDetect0/COOLING
- added copper zone on B.Cu, net /RelayAndRingDetect1/COOLING
- added copper zone on F.Cu, net /RelayAndRingDetect1/COOLING
- added copper zone on B.Cu, net /RelayAndRingDetect10/COOLING
- added copper zone on F.Cu, net /RelayAndRingDetect10/COOLING
- added copper zone on B.Cu, net /RelayAndRingDetect11/COOLING
- added copper zone on F.Cu, net /RelayAndRingDetect11/COOLING
- added copper zone on B.Cu, net /RelayAndRingDetect2/COOLING
- added copper zone on F.Cu, net /RelayAndRingDetect2/COOLING
- added copper zone on B.Cu, net /RelayAndRingDetect3/COOLING
- added copper zone on F.Cu, net /RelayAndRingDetect3/COOLING
- added copper zone on B.Cu, net /RelayAndRingDetect4/COOLING
- added copper zone on F.Cu, net /RelayAndRingDetect4/COOLING
- added copper zone on B.Cu, net /RelayAndRingDetect5/COOLING
- added copper zone on F.Cu, net /RelayAndRingDetect5/COOLING
- added copper zone on B.Cu, net /RelayAndRingDetect6/COOLING
- added copper zone on F.Cu, net /RelayAndRingDetect6/COOLING
- added copper zone on B.Cu, net /RelayAndRingDetect7/COOLING
- added copper zone on F.Cu, net /RelayAndRingDetect7/COOLING
- added copper zone on B.Cu, net /RelayAndRingDetect8/COOLING
- added copper zone on F.Cu, net /RelayAndRingDetect8/COOLING
- added copper zone on B.Cu, net /RelayAndRingDetect9/COOLING
- added copper zone on F.Cu, net /RelayAndRingDetect9/COOLING

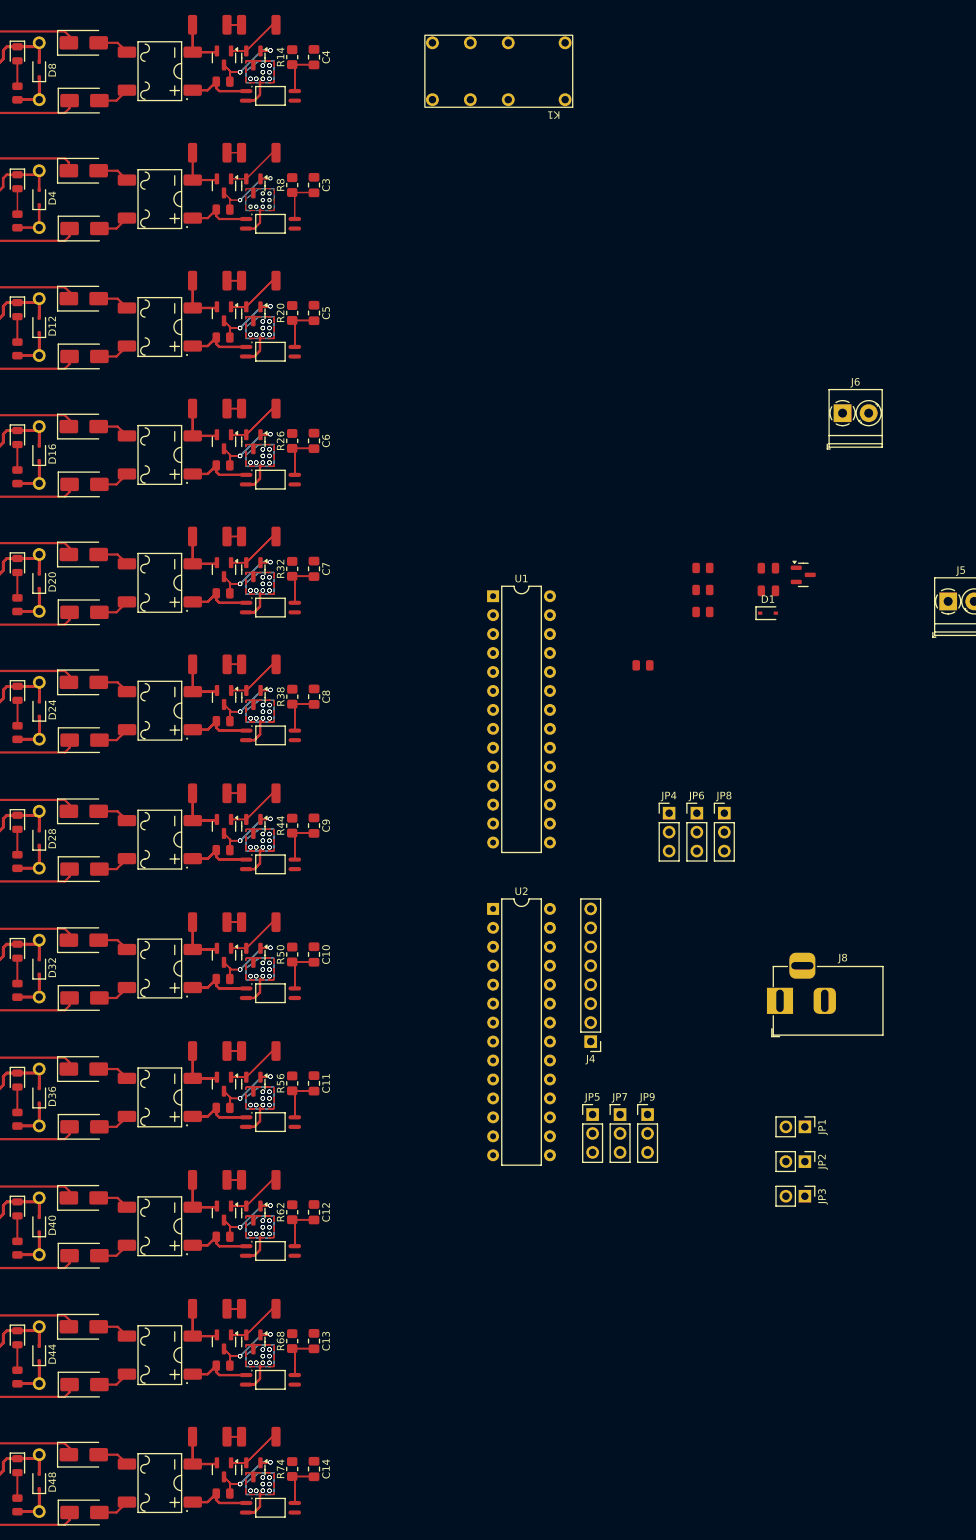
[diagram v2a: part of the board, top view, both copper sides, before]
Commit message: fixed some annotation error
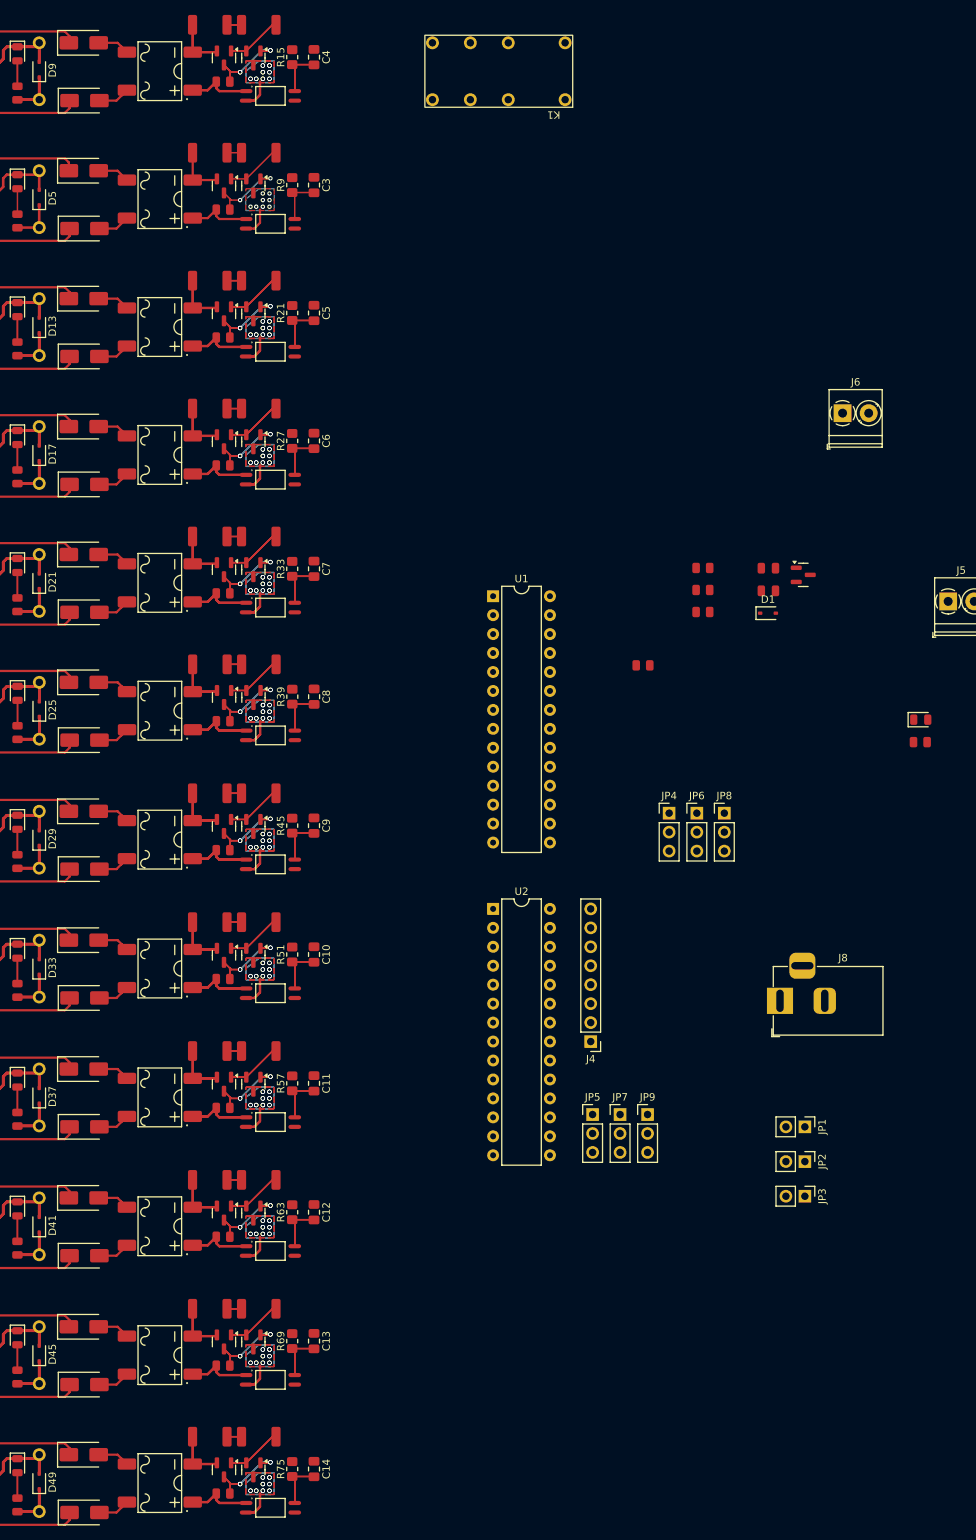
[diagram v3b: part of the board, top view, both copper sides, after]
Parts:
- added D2: Yellow, PCM_JLCPCB:D_0805, F.Cu at (204.5, 98.3)
- added R2: 2.2kΩ, PCM_JLCPCB:R_0805, F.Cu at (204.4, 101.3)
- renumbered D9 to D10, D10 to D11, D11 to D12, D12 to D13, D13 to D14, D14 to D15, D15 to D16, D16 to D17, D17 to D18, D18 to D19, D19 to D20, D20 to D21, D21 to D22, D22 to D23, D23 to D24, D24 to D25, D25 to D26, D26 to D27, D27 to D28, D28 to D29, D2 to D3, D29 to D30, D30 to D31, D31 to D32, D32 to D33, D33 to D34, D34 to D35, D35 to D36, D36 to D37, D37 to D38, D38 to D39, D3 to D4, D39 to D40, D40 to D41, D41 to D42, D42 to D43, D43 to D44, D44 to D45, D45 to D46, D46 to D47, D47 to D48, D48 to D49, D4 to D5, D49 to D50, D5 to D6, D6 to D7, D7 to D8, D8 to D9, R9 to R10, R10 to R11, R11 to R12, R12 to R13, R13 to R14, R14 to R15, R15 to R16, R16 to R17, R17 to R18, R18 to R19, R19 to R20, R20 to R21, R21 to R22, R22 to R23, R23 to R24, R24 to R25, R25 to R26, R26 to R27, R27 to R28, R28 to R29, R2 to R3, R29 to R30, R30 to R31, R31 to R32, R32 to R33, R33 to R34, R34 to R35, R35 to R36, R36 to R37, R37 to R38, R38 to R39, R3 to R4, R39 to R40, R40 to R41, R41 to R42, R42 to R43, R43 to R44, R44 to R45, R45 to R46, R46 to R47, R47 to R48, R48 to R49, R4 to R5, R49 to R50, R50 to R51, R51 to R52, R52 to R53, R53 to R54, R54 to R55, R55 to R56, R56 to R57, R57 to R58, R58 to R59, R5 to R6, R59 to R60, R60 to R61, R61 to R62, R62 to R63, R63 to R64, R64 to R65, R65 to R66, R66 to R67, R67 to R68, R68 to R69, R6 to R7, R69 to R70, R70 to R71, R71 to R72, R72 to R73, R73 to R74, R74 to R75, R75 to R76, R76 to R77, R7 to R8, R8 to R9

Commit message: more layout stuff
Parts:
- removed JP1, JP2, JP3: Jumper_2_Small_Open, Connector_PinHeader_2.54mm:PinHeader_1x02_P2.54mm_Vertical
- J4: value Expansion Hdr. -> Conn_01x09_Pin; footprint Connector_PinHeader_2.54mm:PinHeader_1x08_P2.54mm_Vertical -> Connector_PinHeader_2.54mm:PinHeader_1x09_P2.54mm_Vertical
- J7: value Conn_01x10_Pin -> EXTENSION HDR.; footprint Connector_PinHeader_2.54mm:PinHeader_1x10_P2.54mm_Vertical -> Connector_PinHeader_2.54mm:PinHeader_1x07_P2.54mm_Vertical
- K1: moved to B.Cu
- moved J7 167.9 mm to (149.4, 187.5), turned to 180 degrees
- moved C1 124.9 mm to (131.8, 191.5), turned to -90 degrees
- moved J8 110.8 mm to (162.3, 27.7)
- moved D2 105.2 mm to (147.3, 9.98), turned to -90 degrees
- moved R2 104.5 mm to (147.3, 13.8), turned to 90 degrees
- moved J4 102.8 mm to (172.0, 39.4), turned to 0 degrees
- moved Q1 81.7 mm to (142.4, 11.7)
- moved D1 79.6 mm to (150.4, 11.9), turned to 90 degrees
- moved R1 76.1 mm to (137.9, 11.7), turned to -90 degrees
- moved J5 75.0 mm to (171.2, 17.2), turned to 90 degrees
- moved C2 63.3 mm to (131.4, 45.8), turned to -90 degrees
- moved JP8 63.3 mm to (155.2, 51.9)
- moved JP4 63.3 mm to (147.8, 51.9)
- moved JP6 63.3 mm to (151.5, 51.9)
- moved U1 58.9 mm to (134.6, 24.3)
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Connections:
- J4 pad 1: Net-(J4-Pin_1) -> +3.3V
- J4 pad 2: Net-(J4-Pin_2) -> /SCL
- J4 pad 3: Net-(J4-Pin_3) -> /SDA
- J4 pad 4: Net-(J4-Pin_4) -> /INTA_1
- J4 pad 5: Net-(J4-Pin_5) -> /INTB_1
- J4 pad 6: Net-(J4-Pin_6) -> /RESET
- J4 pad 7: Net-(J4-Pin_7) -> /INTB_2
- J4 pad 8: Net-(J4-Pin_8) -> /INTA_2
- J7 pad 1: /SDA -> /GPA0
- J7 pad 2: /SCL -> /GPA1
- J7 pad 3: /RESET -> /GPA2
- J7 pad 4: /INTA_1 -> /GPA3
- J7 pad 5: /INTB_1 -> /GPA4
- J7 pad 6: /INTA_2 -> /GPA5
- J7 pad 7: /INTB_2 -> /GPA6
- U1 pad 21: /RING_4 -> /RING_7
- U1 pad 22: /SEL_PORT_4 -> /SEL_PORT_7
- U1 pad 23: /RING_5 -> /RING_6
- U1 pad 24: /SEL_PORT_5 -> /SEL_PORT_6
- U1 pad 25: /RING_6 -> /RING_5
- U1 pad 26: /SEL_PORT_6 -> /SEL_PORT_5
- U1 pad 27: /RING_7 -> /RING_4
- U1 pad 28: /SEL_PORT_7 -> /SEL_PORT_4
- U2 pad 21: Net-(J4-Pin_1) -> /GPA0
- U2 pad 22: Net-(J4-Pin_2) -> /GPA1
- U2 pad 23: Net-(J4-Pin_3) -> /GPA2
- U2 pad 24: Net-(J4-Pin_4) -> /GPA3
- U2 pad 25: Net-(J4-Pin_5) -> /GPA4
- U2 pad 26: Net-(J4-Pin_6) -> /GPA5
- U2 pad 27: Net-(J4-Pin_7) -> /GPA6
- U2 pad 28: Net-(J4-Pin_8) -> /SEL_FUNC
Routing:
- net +12V: track 135.9 -> 607.8 mm
- net /SCL: track 0.00 -> 209.4 mm
- net /SDA: track 0.00 -> 208.4 mm
- net /RESET: track 0.00 -> 199.4 mm, vias 0 -> 1
- net /INTB_2: track 0.00 -> 187.6 mm
- net /SEL_FUNC: track 0.00 -> 183.9 mm, vias 0 -> 4
- net /SEL_PORT_6: track 6.43 -> 188.7 mm, vias 0 -> 1
- net /INTA_2: track 0.00 -> 181.4 mm
- net /SEL_PORT_7: track 6.43 -> 176.3 mm, vias 0 -> 1
- net /SEL_PORT_5: track 6.43 -> 168.3 mm, vias 0 -> 1
- net GND: track 0.00 -> 149.8 mm, vias 0 -> 42
- net /SEL_PORT_4: track 6.43 -> 147.4 mm, vias 0 -> 1
- net /RING_5: track 13.3 -> 114.0 mm, vias 0 -> 1
- net /RING_7: track 13.3 -> 112.8 mm, vias 0 -> 1
- net /RelayAndRingDetect0/AUDIO_A: track 212.4 -> 307.7 mm
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- added copper zone on B.Cu, net +3.3V
- added copper zone on F.Cu, net +3.3V
- added copper zone on B.Cu, net GND
- added copper zone on F.Cu, net GND
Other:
- board outline added: 147.4 x 208.5 mm
